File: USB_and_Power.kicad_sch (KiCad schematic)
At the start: 33 parts, among them J3 USB_C_Receptacle_USB2.0_16P, U2 TLV61070ADBV, U3 BQ24074RGT, U4 82400102, U5 TPS63031DSK, U6 FUSB303BTMX

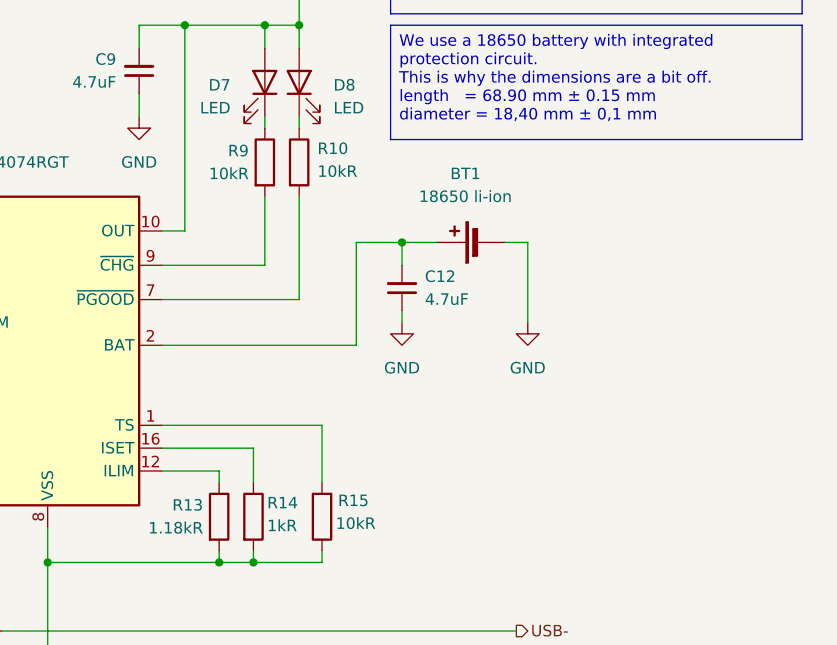
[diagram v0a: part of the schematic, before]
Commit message: Added +BAT and GND Pad to design
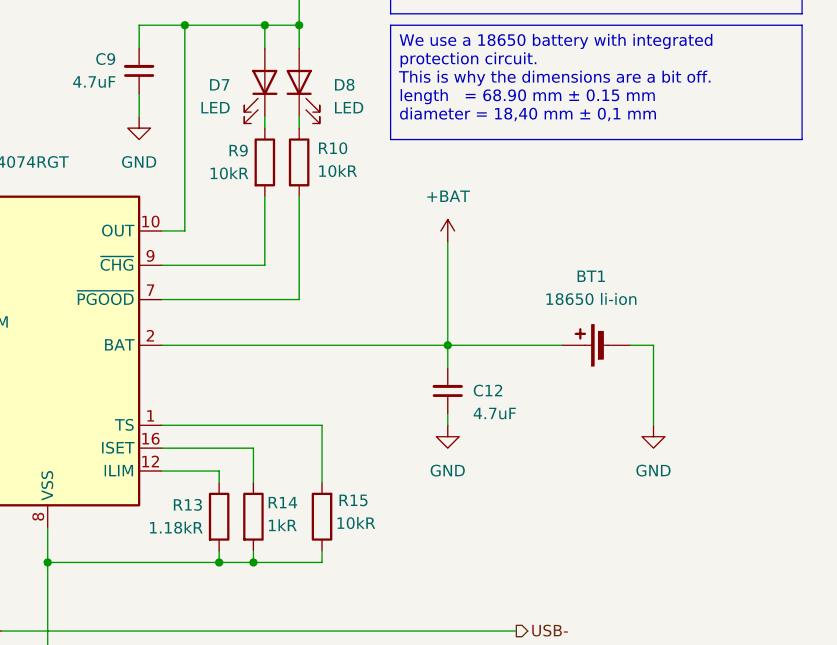
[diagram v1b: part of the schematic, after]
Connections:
- net +BAT: now reaches BT1.1 (+), C12.2, U3.2 (BAT), U3.3 (BAT)
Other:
- moved on the sheet: BT1, C12
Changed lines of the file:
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@@
 	)
 	(junction
-		(at 128.27 59.69)
-		(diameter 0)
-		(color 255 0 255 1)
-	)
-	(junction
 		(at 88.9 95.25)
 		(diameter 0)
@@
 	)
 	(junction
+		(at 133.35 71.12)
+		(diameter 0)
+		(color 255 0 255 1)
+	)
+	(junction
 		(at 88.9 105.41)
 		(diameter 0)
@@
 	(wire
 		(pts
-			(xy 128.27 59.69) (xy 132.08 59.69)
-		)
-		(stroke
-			(width 0.3048)
-			(type default)
-			(color 255 0 255 1)
-		)
-	)
-	(wire
-		(pts
 			(xy 69.85 68.58) (xy 69.85 71.12)
 		)
@@
 	(wire
 		(pts
-			(xy 128.27 59.69) (xy 128.27 62.23)
+			(xy 133.35 71.12) (xy 133.35 73.66)
 		)
 		(stroke
@@
 	(wire
 		(pts
-			(xy 142.24 68.58) (xy 142.24 59.69)
+			(xy 156.21 80.01) (xy 156.21 71.12)
 		)
 		(stroke
@@
 	(wire
 		(pts
-			(xy 128.27 67.31) (xy 128.27 68.58)
+			(xy 133.35 78.74) (xy 133.35 80.01)
 		)
 		(stroke
@@
 	(wire
 		(pts
+			(xy 133.35 59.69) (xy 133.35 71.12)
+		)
+		(stroke
+			(width 0.3048)
+			(type default)
+			(color 255 0 255 1)
+		)
+	)
+	(wire
+		(pts
 			(xy 243.84 73.66) (xy 227.33 73.66)
 		)
@@
 	(wire
 		(pts
-			(xy 123.19 71.12) (xy 123.19 59.69)
-		)
-		(stroke
-			(width 0.3048)
-			(type default)
-			(color 255 0 255 1)
-		)
-	)
-	(wire
-		(pts
 			(xy 58.42 139.7) (xy 77.47 139.7)
 		)
@@
 	(wire
 		(pts
-			(xy 101.6 71.12) (xy 123.19 71.12)
+			(xy 101.6 71.12) (xy 133.35 71.12)
 		)
 		(stroke
@@
 	(wire
 		(pts
-			(xy 123.19 59.69) (xy 128.27 59.69)
+			(xy 205.74 35.56) (xy 205.74 34.29)
 		)
 		(stroke
 			(width 0.3048)
 			(type default)
-			(color 255 0 255 1)
+			(color 0 132 132 1)
 		)
 	)
 	(wire
 		(pts
-			(xy 205.74 35.56) (xy 205.74 34.29)
+			(xy 133.35 71.12) (xy 146.05 71.12)
 		)
 		(stroke
 			(width 0.3048)
 			(type default)
-			(color 0 132 132 1)
+			(color 255 0 255 1)
 		)
 	)
@@
 	(wire
 		(pts
-			(xy 142.24 59.69) (xy 139.7 59.69)
+			(xy 156.21 71.12) (xy 153.67 71.12)
 		)
 		(stroke
@@
 	(symbol
 		(lib_id "Device:Battery_Cell")
-		(at 137.16 59.69 90)
+		(at 151.13 71.12 90)
 		(unit 1)
 		(exclude_from_sim no)
@@
 		(fields_autoplaced yes)
 		(property "Reference" "BT1"
-			(at 135.3185 52.07 90)
+			(at 149.2885 63.5 90)
 			(effects
 				(font
@@
 		)
 		(property "Value" "18650 li-ion"
-			(at 135.3185 54.61 90)
+			(at 149.2885 66.04 90)
 			(effects
 				(font
@@
 		)
 		(property "Footprint" "Battery:BatteryHolder_MPD_BH-18650-PC"
-			(at 135.636 59.69 90)
+			(at 149.606 71.12 90)
 			(effects
 				(font
@@
 		)
 		(property "Datasheet" "~"
-			(at 135.636 59.69 90)
+			(at 149.606 71.12 90)
 			(effects
 				(font
@@
 		)
 		(property "Description" "Single-cell battery"
-			(at 137.16 59.69 0)
+			(at 151.13 71.12 0)
 			(effects
 				(font
@@
 	(symbol
 		(lib_id "power:GND")
-		(at 142.24 68.58 0)
+		(at 156.21 80.01 0)
 		(unit 1)
 		(exclude_from_sim no)
@@
 		(fields_autoplaced yes)
 		(property "Reference" "#PWR024"
-			(at 142.24 74.93 0)
+			(at 156.21 86.36 0)
 			(effects
 				(font
@@
 		)
 		(property "Value" "GND"
-			(at 142.24 73.66 0)
+			(at 156.21 85.09 0)
 			(effects
 				(font
@@
 		)
 		(property "Footprint" ""
-			(at 142.24 68.58 0)
+			(at 156.21 80.01 0)
 			(effects
 				(font
@@
 		)
 		(property "Datasheet" ""
-			(at 142.24 68.58 0)
+			(at 156.21 80.01 0)
 			(effects
 				(font
@@
 		)
 		(property "Description" "Power symbol creates a global label with name \"GND\" , ground"
-			(at 142.24 68.58 0)
+			(at 156.21 80.01 0)
 			(effects
 				(font
@@
 	)
 	(symbol
-		(lib_id "Device:C_Small")
-		(at 128.27 64.77 180)
+		(lib_id "power:+1V0")
+		(at 133.35 59.69 0)
 		(unit 1)
 		(exclude_from_sim no)
@@
 		(dnp no)
 		(fields_autoplaced yes)
+		(property "Reference" "#PWR050"
+			(at 133.35 63.5 0)
+			(effects
+				(font
+					(size 1.27 1.27)
+				)
+				(hide yes)
+			)
+		)
+		(property "Value" "+BAT"
+			(at 133.35 54.61 0)
+			(effects
+				(font
+					(size 1.27 1.27)
+				)
+			)
+		)
+		(property "Footprint" ""
+			(at 133.35 59.69 0)
+			(effects
+				(font
+					(size 1.27 1.27)
+				)
+				(hide yes)
+			)
+		)
+		(property "Datasheet" ""
+			(at 133.35 59.69 0)
+			(effects
+				(font
+					(size 1.27 1.27)
+				)
+				(hide yes)
+			)
+		)
+		(property "Description" "Power symbol creates a global label with name \"+1V0\""
+			(at 133.35 59.69 0)
+			(effects
+				(font
+					(size 1.27 1.27)
+				)
+				(hide yes)
+			)
+		)
+		(pin "1"
+		)
+		(instances
+			(project ""
+				(path "/98695d9f-8521-4f7d-bb41-f22c1215a8e7/de25fb69-79bf-4de2-a7cc-36507c8760b8"
+					(reference "#PWR050")
+					(unit 1)
+				)
+			)
+		)
+	)
+	(symbol
+		(lib_id "Device:C_Small")
+		(at 133.35 76.2 180)
+		(unit 1)
+		(exclude_from_sim no)
+		(in_bom yes)
+		(on_board yes)
+		(dnp no)
 		(property "Reference" "C12"
-			(at 130.81 63.4935 0)
+			(at 136.144 76.2 0)
 			(effects
 				(font
@@
 		)
 		(property "Value" "4.7uF"
-			(at 130.81 66.0335 0)
+			(at 136.144 78.74 0)
 			(effects
 				(font
@@
 		)
 		(property "Footprint" "Capacitor_SMD:C_0805_2012Metric_Pad1.18x1.45mm_HandSolder"
-			(at 128.27 64.77 0)
+			(at 133.35 76.2 0)
 			(effects
 				(font
@@
 		)
 		(property "Datasheet" "~"
-			(at 128.27 64.77 0)
+			(at 133.35 76.2 0)
 			(effects
 				(font
@@
 		)
 		(property "Description" "Unpolarized capacitor, small symbol"
-			(at 128.27 64.77 0)
+			(at 133.35 76.2 0)
 			(effects
 				(font
@@
 	(symbol
 		(lib_id "power:GND")
-		(at 128.27 68.58 0)
+		(at 133.35 80.01 0)
 		(unit 1)
 		(exclude_from_sim no)
@@
 		(fields_autoplaced yes)
 		(property "Reference" "#PWR023"
-			(at 128.27 74.93 0)
+			(at 133.35 86.36 0)
 			(effects
 				(font
@@
 		)
 		(property "Value" "GND"
-			(at 128.27 73.66 0)
+			(at 133.35 85.09 0)
 			(effects
 				(font
@@
 		)
 		(property "Footprint" ""
-			(at 128.27 68.58 0)
+			(at 133.35 80.01 0)
 			(effects
 				(font
@@
 		)
 		(property "Datasheet" ""
-			(at 128.27 68.58 0)
+			(at 133.35 80.01 0)
 			(effects
 				(font
@@
 		)
 		(property "Description" "Power symbol creates a global label with name \"GND\" , ground"
-			(at 128.27 68.58 0)
+			(at 133.35 80.01 0)
 			(effects
 				(font
